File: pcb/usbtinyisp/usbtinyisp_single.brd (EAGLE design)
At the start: 44 x 36 mm, 26 parts, among them IC1 ATTINY2313-20P, IC2 74LVX125D, Q1 12000

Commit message: replace mounting pads
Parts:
- U$1, U$2, U$3, U$4: device holes:3,2 -> holes:3,2-PAD
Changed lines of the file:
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@@
 <param name="mdViaViaSameLayer" value="8mil"/>
 <param name="mnLayersViaInSmd" value="2"/>
-<param name="mdCopperDimension" value="1.7mm"/>
+<param name="mdCopperDimension" value="40mil"/>
 <param name="mdDrill" value="8mil"/>
 <param name="mdSmdStop" value="0mil"/>
@@
 <element name="IC2" library="74xx-eu" package="SO14" value="74LVX125D" x="34.29" y="22.86" rot="MR270"/>
 <element name="C2" library="rcl" package="E2,5-7" value="100u" x="16.51" y="6.35" rot="R180"/>
-<element name="U$1" library="holes" package="3,2" value="" x="4" y="4"/>
-<element name="U$2" library="holes" package="3,2" value="" x="40" y="4"/>
-<element name="U$3" library="holes" package="3,2" value="" x="40" y="32"/>
-<element name="U$4" library="holes" package="3,2" value="" x="4" y="32"/>
+<element name="U$1" library="holes" package="3,2-PAD" value="" x="4" y="4"/>
+<element name="U$2" library="holes" package="3,2-PAD" value="" x="40" y="4"/>
+<element name="U$3" library="holes" package="3,2-PAD" value="" x="40" y="32"/>
+<element name="U$4" library="holes" package="3,2-PAD" value="" x="4" y="32"/>
 <element name="Q1" library="crystal" package="HC49U-V" value="12000" x="11.43" y="24.13" rot="R90">
 <attribute name="OC_NEWARK" value="unknown" x="11.43" y="24.13" size="1.778" layer="27" rot="R90" display="off"/>

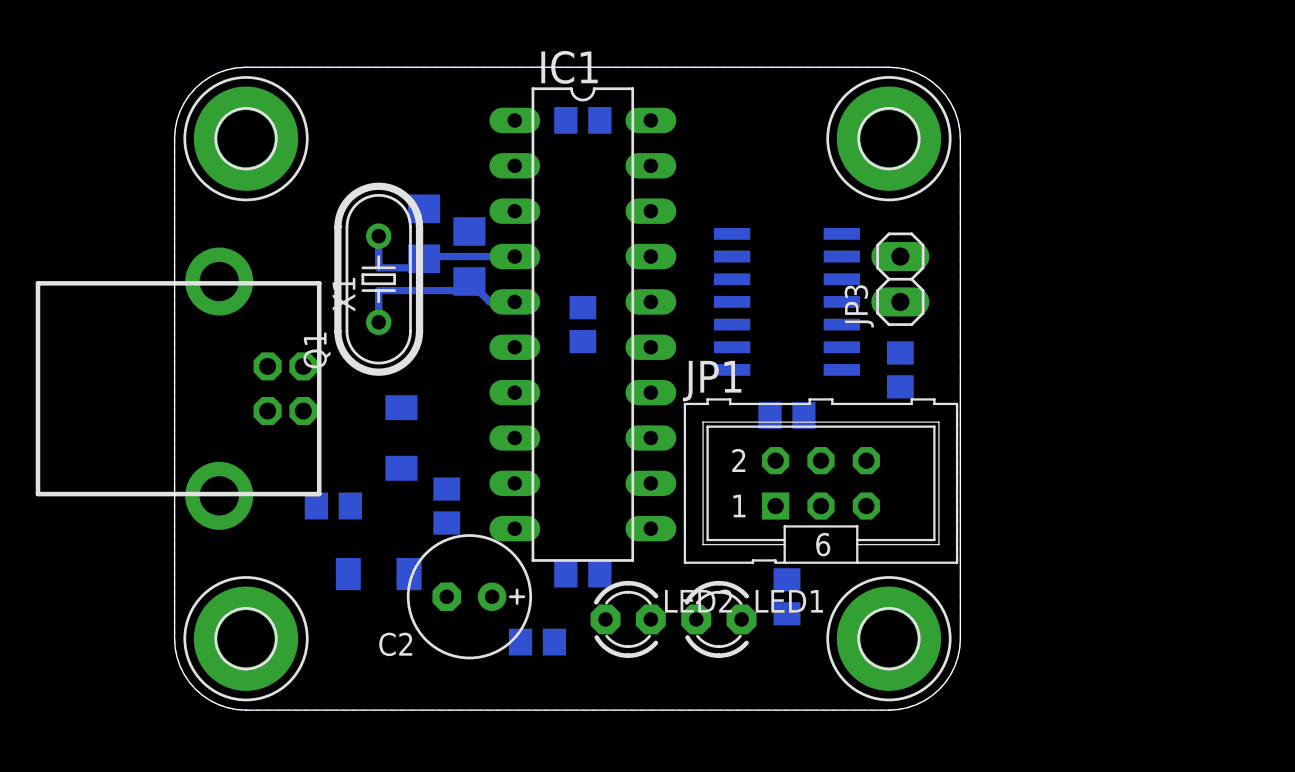
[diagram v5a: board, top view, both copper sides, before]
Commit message: swapped some gates and moved all parts around
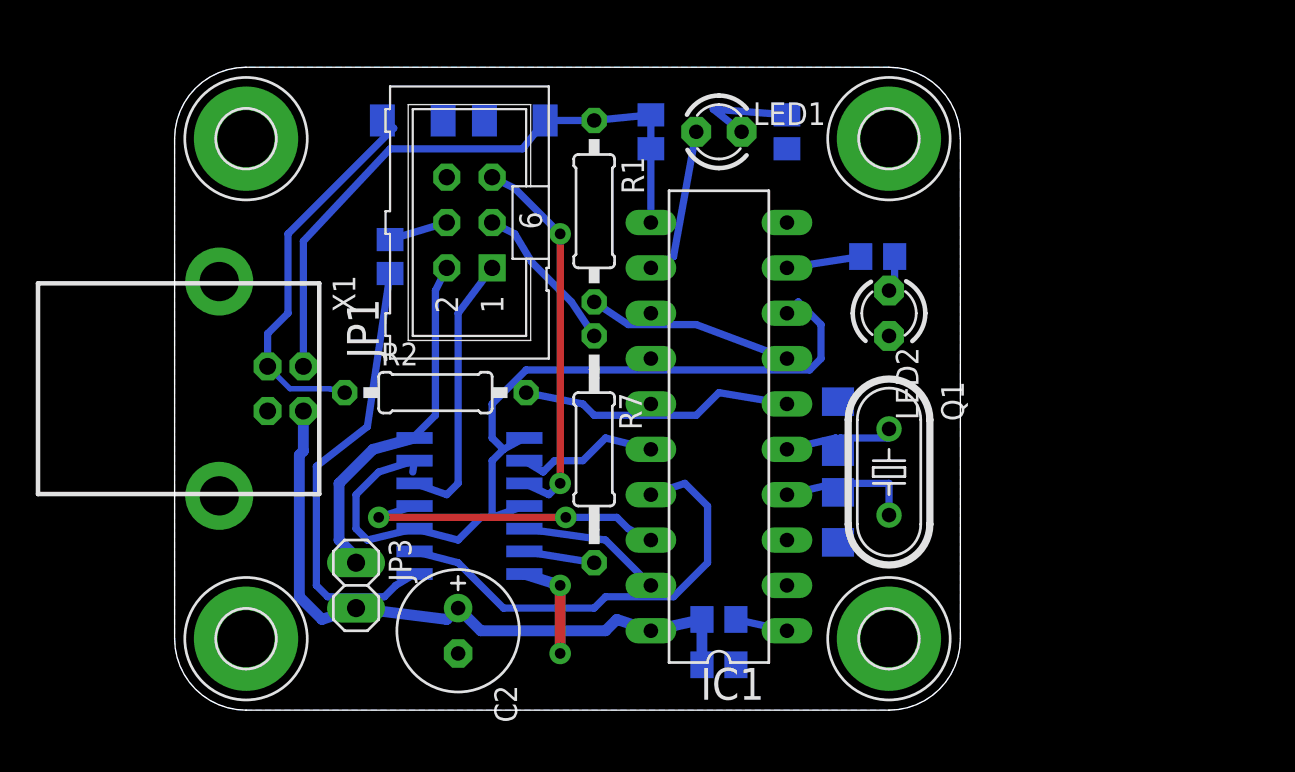
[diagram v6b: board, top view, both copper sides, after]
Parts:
- R1, R2: device rcl:R0805 -> rcl:0207/10
- R7: device rcl:R0805 -> rcl:0207/12
- moved JP3 35.0 mm to (10.2, 6.99), turned to 270 degrees
- moved Q1 30.5 mm to (40.0, 13.3), turned to 270 degrees
- moved R10 29.0 mm to (30.5, 5.08), turned to 0 degrees
- moved R5 28.8 mm to (39.4, 25.4)
- moved C3 28.1 mm to (37.1, 10.8), turned to 270 degrees
- moved LED1 27.3 mm to (30.5, 32.4)
- moved R6 26.0 mm to (34.3, 32.4), turned to 90 degrees
- moved D1 25.5 mm to (13.3, 33.0)
- moved R3 25.1 mm to (26.7, 32.4), turned to 270 degrees
- moved JP1 24.5 mm to (16.5, 27.3), turned to 90 degrees
- moved R4 23.9 mm to (12.1, 25.4), turned to 270 degrees
- moved C4 22.7 mm to (37.1, 15.9)
- moved LED2 22.5 mm to (40.0, 22.2), turned to 270 degrees
- moved IC2 21.1 mm to (16.5, 11.4)
- moved C1 20.5 mm to (30.5, 2.54), turned to 180 degrees
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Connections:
- net N$12: now also IC2.6; no longer IC2.3
- net RST: now also IC2.3; no longer IC2.6
- net RST': now also IC2.2; no longer IC2.5
- net SCK': now also IC2.5; no longer IC2.2
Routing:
- net N$15: track 0.00 -> 49.2 mm
- net VCC: track 0.00 -> 37.5 mm
- net N$1: track 0.00 -> 29.5 mm
- net MOSI': track 0.00 -> 25.6 mm
- net N$13: track 0.00 -> 25.2 mm
- net N$2: track 0.00 -> 21.9 mm
- net RST: track 0.00 -> 21.4 mm, vias 0 -> 2
- net N$14: track 0.00 -> 20.1 mm
- net MISO': track 0.00 -> 17.8 mm, vias 0 -> 2
- net MISO: track 0.00 -> 15.5 mm
- net N$6: track 0.00 -> 15.5 mm
- net N$3: track 0.00 -> 11.5 mm
- net SCK: track 0.00 -> 8.70 mm
- net N$7: track 0.00 -> 8.52 mm
- net SCK': track 0.00 -> 8.18 mm
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
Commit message: routed
ready for soldering (first test)
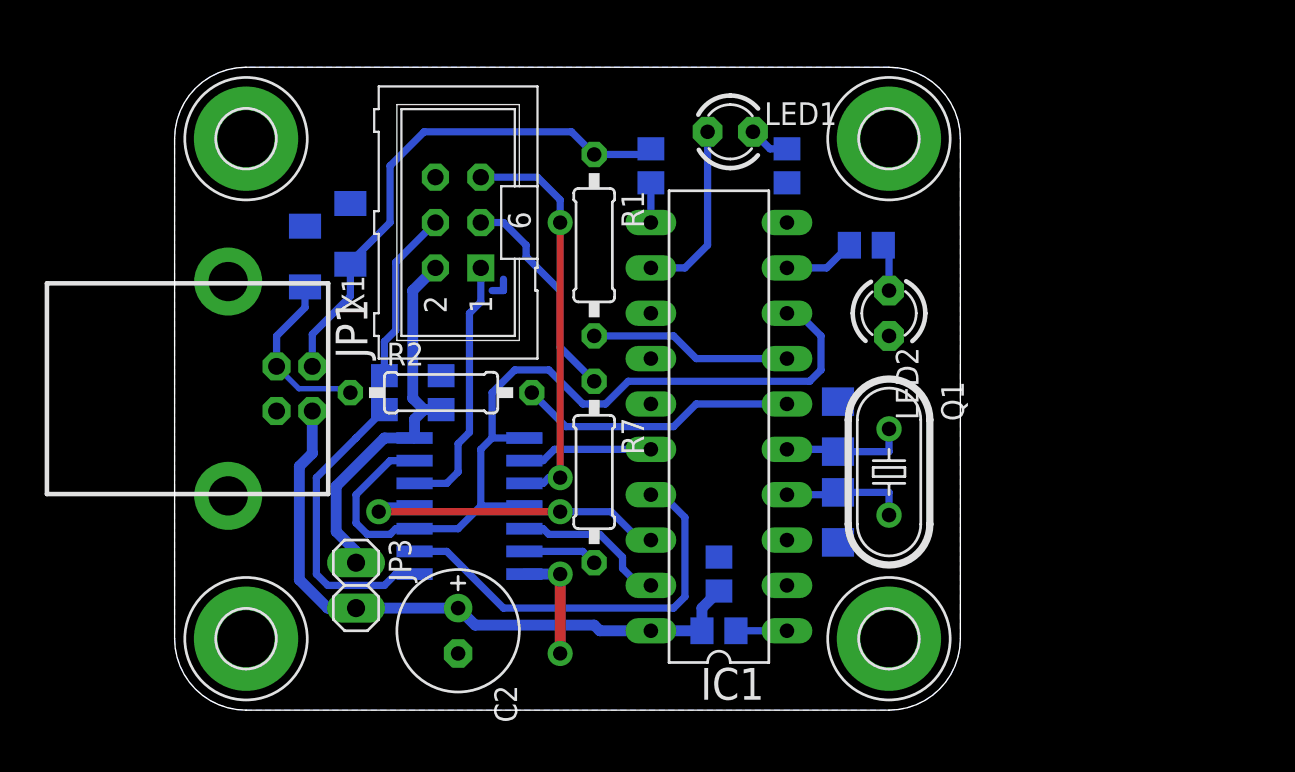
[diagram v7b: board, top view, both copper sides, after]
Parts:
- added C5: 100n, rcl:C0805
- R7: device rcl:0207/12 -> rcl:0207/10
- moved D2 11.2 mm to (9.84, 26.7), turned to 90 degrees
- moved D1 9.72 mm to (7.30, 25.4), turned to 90 degrees
- moved R4 7.63 mm to (11.7, 17.8)
- moved C1 5.08 mm to (30.5, 7.62), turned to 90 degrees
- moved R1 1.91 mm to (23.5, 26.0)
- moved R3 1.90 mm to (26.7, 30.5)
- moved R6 1.90 mm to (34.3, 30.5)
- moved R7 1.27 mm to (23.5, 13.3)
- moved R5 0.90 mm to (38.7, 26.0)
- moved JP1 0.64 mm to (15.9, 27.3)
- moved R10 0.63 mm to (30.5, 4.45)
- moved LED1 0.63 mm to (31.1, 32.4)
- moved X1 0.50 mm to (3.00, 18.0)
- moved R2 0.32 mm to (14.9, 17.8)
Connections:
- removed net N$14: IC2.14, JP1.2, JP3.1
- new net VTARGET: C5.1, IC2.14, JP1.2, JP3.1
- net GND: now also C5.2
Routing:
- net VTARGET: track 0.00 -> 21.7 mm
- net N$14: track 20.1 -> 0.00 mm
- net N$2: track 21.9 -> 9.85 mm
- net N$13: track 25.2 -> 16.8 mm
- net MOSI: track 3.32 -> 9.76 mm
- net N$8: track 6.18 -> 2.30 mm
- net SCK: track 8.70 -> 12.3 mm
- net N$16: track 5.40 -> 2.23 mm
- net MOSI': track 25.6 -> 23.6 mm
- net N$7: track 8.52 -> 10.1 mm
- net VCC: track 37.5 -> 36.1 mm
- net XTAL2: track 8.35 -> 7.04 mm
- net RST: track 21.4 -> 22.7 mm
- net N$5: track 0.00 -> 1.27 mm
- net MISO: track 15.5 -> 14.7 mm
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
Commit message: add text, license, and readme
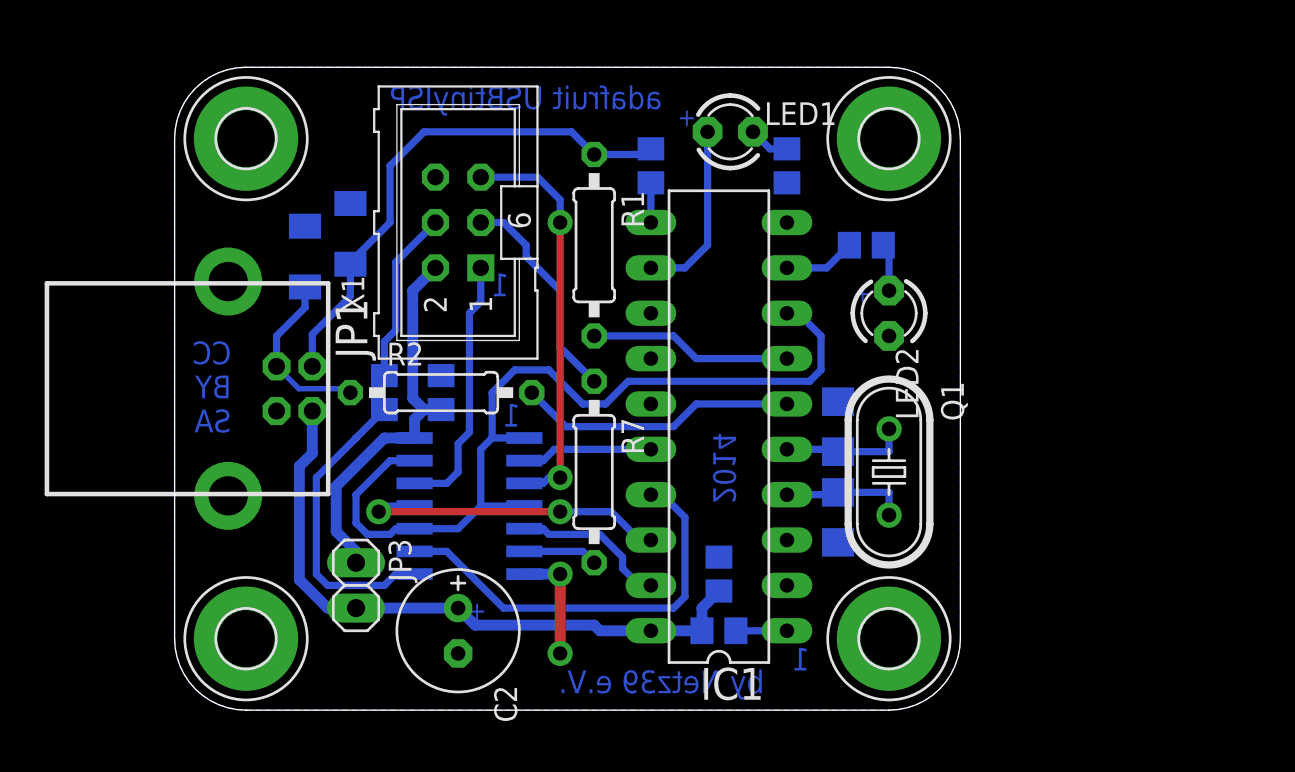
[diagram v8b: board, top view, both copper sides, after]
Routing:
- net N$5: track 1.27 -> 0.00 mm
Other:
- board text added: "+"
- board text added: "1"
- board text added: "2014"
- board text added: "CC BY SA"
- board text added: "adafruit USBtinyISP"
- board text added: "by Netz39 e.V."
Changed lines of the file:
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@@
 <setting verticaltext="up"/>
 </settings>
-<grid distance="12.5" unitdist="mil" unit="mil" style="dots" multiple="1" display="no" altdistance="6.25" altunitdist="mil" altunit="mil"/>
+<grid distance="25" unitdist="mil" unit="mil" style="dots" multiple="1" display="yes" altdistance="12.5" altunitdist="mil" altunit="mil"/>
 <layers>
 <layer number="1" name="Top" color="4" fill="1" visible="yes" active="yes"/>
@@
 <wire x1="44" y1="4" x2="40" y2="0" width="0" layer="20" curve="-90"/>
 <wire x1="4" y1="0" x2="0" y2="4" width="0" layer="20" curve="-90"/>
+<text x="33.02" y="0.9525" size="1.27" layer="16" font="vector" ratio="15" rot="MR0">by Netz39 e.V.</text>
+<text x="27.305" y="33.655" size="1.27" layer="16" font="vector" ratio="15" rot="MR0">adafruit USBtinyISP</text>
+<text x="31.4325" y="15.5575" size="1.27" layer="16" font="vector" ratio="15" rot="MR270">2014</text>
+<text x="3.175" y="15.5575" size="1.27" layer="16" font="vector" ratio="15" rot="MR0">CC
+BY
+SA</text>
+<text x="19.3675" y="15.875" size="1.27" layer="16" font="vector" ratio="13" rot="MR0">1</text>
+<text x="35.56" y="2.2225" size="1.27" layer="16" font="vector" ratio="13" rot="MR0">1</text>
+<text x="18.7325" y="23.1775" size="1.27" layer="16" font="vector" ratio="13" rot="MR0">1</text>
+<text x="17.4625" y="5.08" size="1.016" layer="16" font="vector" ratio="13" rot="MR0">+</text>
+<text x="39.0525" y="22.86" size="1.016" layer="16" font="vector" ratio="13" rot="MR0">+</text>
+<text x="29.21" y="32.7025" size="1.016" layer="16" font="vector" ratio="13" rot="MR0">+</text>
 </plain>
 <attributes>
@@
 <signal name="N$4">
 </signal>
-<signal name="N$5">
-<wire x1="18.415" y1="24.13" x2="18.415" y2="23.495" width="0.4064" layer="16"/>
-<wire x1="17.78" y1="23.495" x2="18.415" y2="23.495" width="0.4064" layer="16"/>
-</signal>
 </signals>
 <errors>
@@
 </board>
 </drawing>
+<compatibility>
+<note version="6.3" minversion="6.2.2" severity="warning">
+Since Version 6.2.2 text objects can contain more than one line,
+which will not be processed correctly with this version.
+</note>
+</compatibility>
 </eagle>
